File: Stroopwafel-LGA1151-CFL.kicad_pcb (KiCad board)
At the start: 2 copper layers, 2 parts

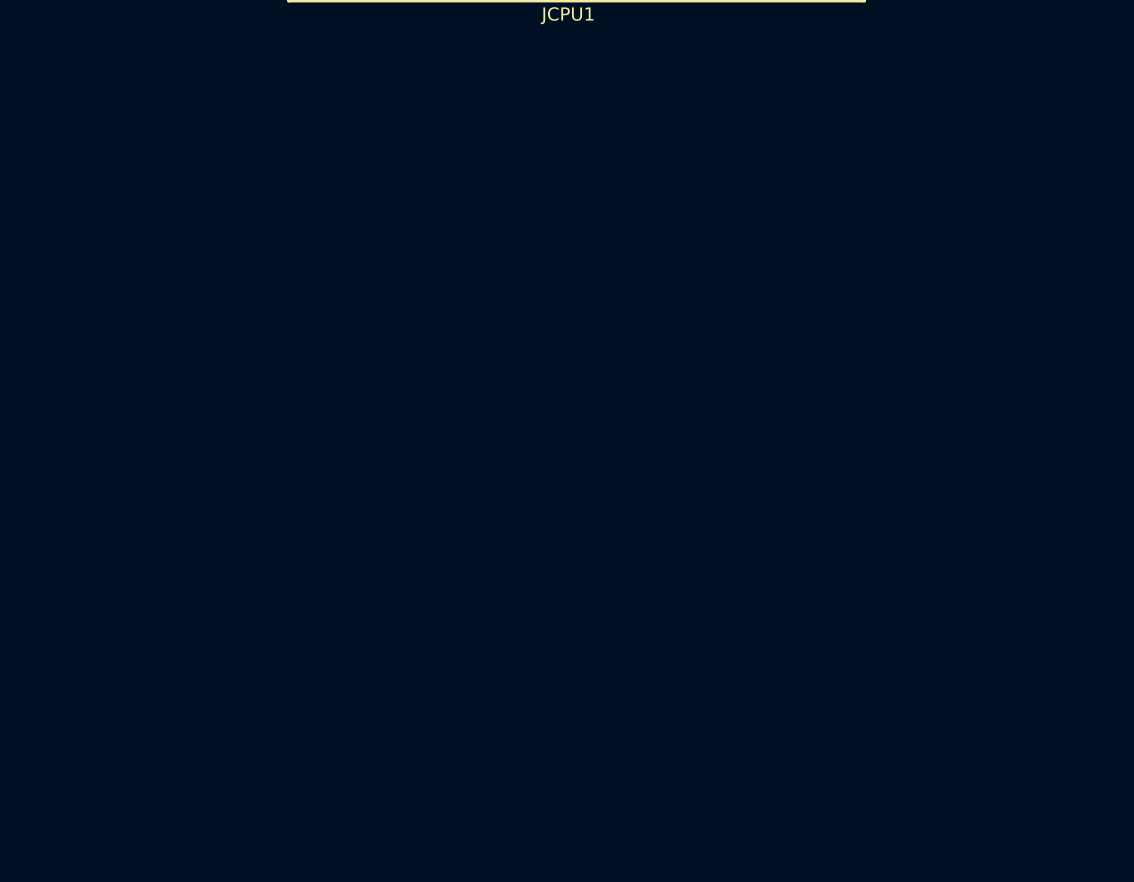
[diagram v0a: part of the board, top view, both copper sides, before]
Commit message: Added sodimm memory slots and mostly hooked them up on the schematic
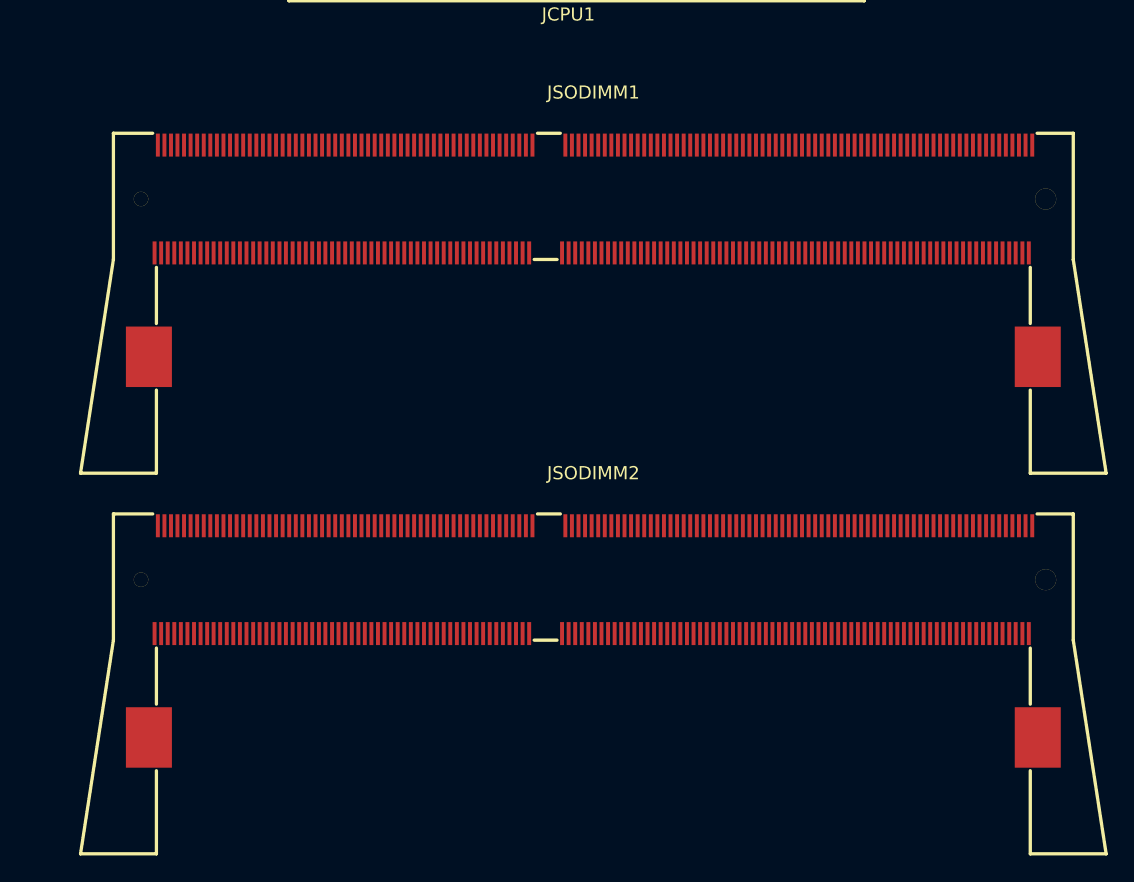
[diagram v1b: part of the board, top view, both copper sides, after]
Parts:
- added JSODIMM1: DDR4-sodimm, A-my-stuff:DDR4-sodimm-std, F.Cu at (201.9, 110.3)
- added JSODIMM2: DDR4-sodimm, A-my-stuff:DDR4-sodimm-std, F.Cu at (201.9, 139.2)
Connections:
- JCPU1 pad AD34: unconnected-(JCPU1B-DDR1_DQ_0/DDR0_DQ_16-PadAD34) -> DDR4_CH1_DQ0
- JCPU1 pad AD35: unconnected-(JCPU1B-DDR1_DQ_1/DDR0_DQ_17-PadAD35) -> DDR4_CH1_DQ1
- JCPU1 pad AE34: unconnected-(JCPU1B-DDR1_DQ_5/DDR0_DQ_21-PadAE34) -> DDR4_CH1_DQ5
- JCPU1 pad AE35: unconnected-(JCPU1B-DDR1_DQ_4/DDR0_DQ_20-PadAE35) -> DDR4_CH1_DQ4
- JCPU1 pad AE37: unconnected-(JCPU1A-DDR0_DQ_1/DDR0_DQ_1-PadAE37) -> DDR4_CH0_DQ1
- JCPU1 pad AE38: unconnected-(JCPU1A-DDR0_DQ_0/DDR0_DQ_0-PadAE38) -> DDR4_CH0_DQ0
- JCPU1 pad AE39: unconnected-(JCPU1A-DDR0_DQ_4/DDR0_DQ_4-PadAE39) -> DDR4_CH0_DQ4
- JCPU1 pad AE40: unconnected-(JCPU1A-DDR0_DQ_5/DDR0_DQ_5-PadAE40) -> DDR4_CH0_DQ5
- JCPU1 pad AE6: unconnected-(JCPU1B-DDR1_DQ_58/DDR1_DQ_58-PadAE6) -> DDR4_CH1_DQ58
- JCPU1 pad AE7: unconnected-(JCPU1B-DDR1_DQ_62/DDR1_DQ_62-PadAE7) -> DDR4_CH1_DQ62
- JCPU1 pad AF34: unconnected-(JCPU1B-DDR1_DQSN_0/DDR0_DQSN_2-PadAF34) -> DDR4_CH1_DQS0-
- JCPU1 pad AF35: unconnected-(JCPU1B-DDR1_DQSP_0/DDR0_DQSP_2-PadAF35) -> DDR4_CH1_DQS0+
- JCPU1 pad AF38: unconnected-(JCPU1A-DDR0_DQSP_0/DDR0_DQSP_0-PadAF38) -> DDR4_CH0_DQS0+
- JCPU1 pad AF39: unconnected-(JCPU1A-DDR0_DQSN_0/DDR0_DQSN_0-PadAF39) -> DDR4_CH0_DQS0-
- JCPU1 pad AF6: unconnected-(JCPU1B-DDR1_DQ_63/DDR1_DQ_63-PadAF6) -> DDR4_CH1_DQ63
- JCPU1 pad AF7: unconnected-(JCPU1B-DDR1_DQ_59/DDR1_DQ_59-PadAF7) -> DDR4_CH1_DQ59
- JCPU1 pad AG34: unconnected-(JCPU1B-DDR1_DQ_6/DDR0_DQ_22-PadAG34) -> DDR4_CH1_DQ6
- JCPU1 pad AG35: unconnected-(JCPU1B-DDR1_DQ_2/DDR0_DQ_18-PadAG35) -> DDR4_CH1_DQ2
- JCPU1 pad AG37: unconnected-(JCPU1A-DDR0_DQ_3/DDR0_DQ_3-PadAG37) -> DDR4_CH0_DQ3
- JCPU1 pad AG38: unconnected-(JCPU1A-DDR0_DQ_2/DDR0_DQ_2-PadAG38) -> DDR4_CH0_DQ2
- JCPU1 pad AG39: unconnected-(JCPU1A-DDR0_DQ_6/DDR0_DQ_6-PadAG39) -> DDR4_CH0_DQ6
- JCPU1 pad AG40: unconnected-(JCPU1A-DDR0_DQ_7/DDR0_DQ_7-PadAG40) -> DDR4_CH0_DQ7
- JCPU1 pad AG6: unconnected-(JCPU1B-DDR1_DQSN_7/DDR1_DQSN_7-PadAG6) -> DDR4_CH1_DQS7-
- JCPU1 pad AG7: unconnected-(JCPU1B-DDR1_DQSP_7/DDR1_DQSP_7-PadAG7) -> DDR4_CH1_DQS7+
- JCPU1 pad AH1: unconnected-(JCPU1A-DDR0_DQ_57/DDR1_DQ_41-PadAH1) -> DDR4_CH0_DQ57
- JCPU1 pad AH2: unconnected-(JCPU1A-DDR0_DQ_59/DDR1_DQ_43-PadAH2) -> DDR4_CH0_DQ59
- JCPU1 pad AH3: unconnected-(JCPU1A-DDR0_DQ_62/DDR1_DQ_46-PadAH3) -> DDR4_CH0_DQ62
- JCPU1 pad AH34: unconnected-(JCPU1B-DDR1_DQ_7/DDR0_DQ_23-PadAH34) -> DDR4_CH1_DQ7
- JCPU1 pad AH35: unconnected-(JCPU1B-DDR1_DQ_3/DDR0_DQ_19-PadAH35) -> DDR4_CH1_DQ3
- JCPU1 pad AH4: unconnected-(JCPU1A-DDR0_DQ_60/DDR1_DQ_44-PadAH4) -> DDR4_CH0_DQ60
- JCPU1 pad AH6: unconnected-(JCPU1B-DDR1_DQ_61/DDR1_DQ_61-PadAH6) -> DDR4_CH1_DQ61
- JCPU1 pad AH7: unconnected-(JCPU1B-DDR1_DQ_60/DDR1_DQ_60-PadAH7) -> DDR4_CH1_DQ60
- JCPU1 pad AJ2: unconnected-(JCPU1A-DDR0_DQSP_7/DDR1_DQSP_5-PadAJ2) -> DDR4_CH0_DQS7+
- JCPU1 pad AJ3: unconnected-(JCPU1A-DDR0_DQSN_7/DDR1_DQSN_5-PadAJ3) -> DDR4_CH0_DQS7-
- JCPU1 pad AJ37: unconnected-(JCPU1A-DDR0_DQ_9/DDR0_DQ_9-PadAJ37) -> DDR4_CH0_DQ9
- JCPU1 pad AJ38: unconnected-(JCPU1A-DDR0_DQ_8/DDR0_DQ_8-PadAJ38) -> DDR4_CH0_DQ8
- JCPU1 pad AJ39: unconnected-(JCPU1A-DDR0_DQ_13/DDR0_DQ_13-PadAJ39) -> DDR4_CH0_DQ13
- JCPU1 pad AJ40: unconnected-(JCPU1A-DDR0_DQ_12/DDR0_DQ_12-PadAJ40) -> DDR4_CH0_DQ12
- JCPU1 pad AJ6: unconnected-(JCPU1B-DDR1_DQ_56/DDR1_DQ_56-PadAJ6) -> DDR4_CH1_DQ56
- JCPU1 pad AJ7: unconnected-(JCPU1B-DDR1_DQ_57/DDR1_DQ_57-PadAJ7) -> DDR4_CH1_DQ57
- JCPU1 pad AK1: unconnected-(JCPU1A-DDR0_DQ_63/DDR1_DQ_47-PadAK1) -> DDR4_CH0_DQ63
- JCPU1 pad AK2: unconnected-(JCPU1A-DDR0_DQ_61/DDR1_DQ_45-PadAK2) -> DDR4_CH0_DQ61
- JCPU1 pad AK3: unconnected-(JCPU1A-DDR0_DQ_56/DDR1_DQ_40-PadAK3) -> DDR4_CH0_DQ56
- JCPU1 pad AK31: unconnected-(JCPU1B-DDR1_DQ_14/DDR0_DQ_30-PadAK31) -> DDR4_CH1_DQ14
- JCPU1 pad AK32: unconnected-(JCPU1B-DDR1_DQ_10/DDR0_DQ_26-PadAK32) -> DDR4_CH1_DQ10
- JCPU1 pad AK33: unconnected-(JCPU1B-DDR1_DQSN_1/DDR0_DQSN_3-PadAK33) -> DDR4_CH1_DQS1-
- JCPU1 pad AK34: unconnected-(JCPU1B-DDR1_DQ_12/DDR0_DQ_28-PadAK34) -> DDR4_CH1_DQ12
- JCPU1 pad AK35: unconnected-(JCPU1B-DDR1_DQ_8/DDR0_DQ_24-PadAK35) -> DDR4_CH1_DQ8
- JCPU1 pad AK38: unconnected-(JCPU1A-DDR0_DQSP_1/DDR0_DQSP_1-PadAK38) -> DDR4_CH0_DQS1+
- JCPU1 pad AK39: unconnected-(JCPU1A-DDR0_DQSN_1/DDR0_DQSN_1-PadAK39) -> DDR4_CH0_DQS1-
- JCPU1 pad AK4: unconnected-(JCPU1A-DDR0_DQ_58/DDR1_DQ_42-PadAK4) -> DDR4_CH0_DQ58
- JCPU1 pad AL10: unconnected-(JCPU1B-DDR1_DQ_49/DDR1_DQ_49-PadAL10) -> DDR4_CH1_DQ49
- JCPU1 pad AL12: unconnected-(JCPU1B-DDR1_DQ_39/DDR1_DQ_23-PadAL12) -> DDR4_CH1_DQ39
- JCPU1 pad AL13: unconnected-(JCPU1B-DDR1_DQ_35/DDR1_DQ_19-PadAL13) -> DDR4_CH1_DQ35
- JCPU1 pad AL16: unconnected-(JCPU1B-DDR1_ODT_1-PadAL16) -> DDR4_CH1_ODT1
- JCPU1 pad AL17: unconnected-(JCPU1B-DDR1_MA_14-PadAL17) -> DDR4_CH1_A14_WE#
- JCPU1 pad AL18: unconnected-(JCPU1B-DDR1_BA_0-PadAL18) -> DDR4_CH1_BA0
- JCPU1 pad AL19: unconnected-(JCPU1B-DDR1_MA_0-PadAL19) -> DDR4_CH1_A0
- JCPU1 pad AL20: unconnected-(JCPU1B-DDR1_PAR-PadAL20) -> DDR4_CH1_Parity
- JCPU1 pad AL22: unconnected-(JCPU1B-DDR1_MA_1-PadAL22) -> DDR4_CH1_A1
- JCPU1 pad AL23: unconnected-(JCPU1B-DDR1_MA_5-PadAL23) -> DDR4_CH1_A5
- JCPU1 pad AL25: unconnected-(JCPU1B-DDR1_ECC_6-PadAL25) -> DDR4_CH1_ECC6
- JCPU1 pad AL26: unconnected-(JCPU1B-DDR1_ECC_7-PadAL26) -> DDR4_CH1_ECC7
- JCPU1 pad AL28: unconnected-(JCPU1B-DDR1_DQ_29/DDR0_DQ_61-PadAL28) -> DDR4_CH1_DQ29
- JCPU1 pad AL29: unconnected-(JCPU1B-DDR1_DQ_24/DDR0_DQ_56-PadAL29) -> DDR4_CH1_DQ24
- JCPU1 pad AL31: unconnected-(JCPU1B-DDR1_DQ_15/DDR0_DQ_31-PadAL31) -> DDR4_CH1_DQ15
- JCPU1 pad AL32: unconnected-(JCPU1B-DDR1_DQ_11/DDR0_DQ_27-PadAL32) -> DDR4_CH1_DQ11
- JCPU1 pad AL33: unconnected-(JCPU1B-DDR1_DQSP_1/DDR0_DQSP_3-PadAL33) -> DDR4_CH1_DQS1+
- JCPU1 pad AL34: unconnected-(JCPU1B-DDR1_DQ_13/DDR0_DQ_29-PadAL34) -> DDR4_CH1_DQ13
- JCPU1 pad AL35: unconnected-(JCPU1B-DDR1_DQ_9/DDR0_DQ_25-PadAL35) -> DDR4_CH1_DQ9
- JCPU1 pad AL37: unconnected-(JCPU1A-DDR0_DQ_11/DDR0_DQ_11-PadAL37) -> DDR4_CH0_DQ11
- JCPU1 pad AL38: unconnected-(JCPU1A-DDR0_DQ_10/DDR0_DQ_10-PadAL38) -> DDR4_CH0_DQ10
- JCPU1 pad AL39: unconnected-(JCPU1A-DDR0_DQ_14/DDR0_DQ_14-PadAL39) -> DDR4_CH0_DQ14
- JCPU1 pad AL40: unconnected-(JCPU1A-DDR0_DQ_15/DDR0_DQ_15-PadAL40) -> DDR4_CH0_DQ15
- JCPU1 pad AL6: unconnected-(JCPU1B-DDR1_DQ_55/DDR1_DQ_55-PadAL6) -> DDR4_CH1_DQ55
- JCPU1 pad AL7: unconnected-(JCPU1B-DDR1_DQ_51/DDR1_DQ_51-PadAL7) -> DDR4_CH1_DQ51
- JCPU1 pad AL8: unconnected-(JCPU1B-DDR1_DQSP_6/DDR1_DQSP_6-PadAL8) -> DDR4_CH1_DQS6+
- JCPU1 pad AL9: unconnected-(JCPU1B-DDR1_DQ_53/DDR1_DQ_53-PadAL9) -> DDR4_CH1_DQ53
- JCPU1 pad AM1: unconnected-(JCPU1A-DDR0_DQ_55/DDR1_DQ_39-PadAM1) -> DDR4_CH0_DQ55
- JCPU1 pad AM10: unconnected-(JCPU1B-DDR1_DQ_48/DDR1_DQ_48-PadAM10) -> DDR4_CH1_DQ48
- JCPU1 pad AM12: unconnected-(JCPU1B-DDR1_DQ_38/DDR1_DQ_22-PadAM12) -> DDR4_CH1_DQ38
- JCPU1 pad AM13: unconnected-(JCPU1B-DDR1_DQ_34/DDR1_DQ_18-PadAM13) -> DDR4_CH1_DQ34
- JCPU1 pad AM16: unconnected-(JCPU1B-DDR1_ODT_0-PadAM16) -> DDR4_CH1_ODT0
- JCPU1 pad AM18: unconnected-(JCPU1B-DDR1_BA_1-PadAM18) -> DDR4_CH1_BA1
- JCPU1 pad AM2: unconnected-(JCPU1A-DDR0_DQ_53/DDR1_DQ_37-PadAM2) -> DDR4_CH0_DQ53
- JCPU1 pad AM20: unconnected-(JCPU1B-DDR1_CKP_0-PadAM20) -> DDR4_CH1_CLK0+
- JCPU1 pad AM21: unconnected-(JCPU1B-DDR1_CKN_0-PadAM21) -> DDR4_CH1_CLK0-
- JCPU1 pad AM22: unconnected-(JCPU1B-DDR1_MA_2-PadAM22) -> DDR4_CH1_A2
- JCPU1 pad AM23: unconnected-(JCPU1B-DDR1_MA_3-PadAM23) -> DDR4_CH1_A3
- JCPU1 pad AM25: unconnected-(JCPU1B-DDR1_ECC_3-PadAM25) -> DDR4_CH1_ECC3
- JCPU1 pad AM26: unconnected-(JCPU1B-DDR1_ECC_2-PadAM26) -> DDR4_CH1_ECC2
- JCPU1 pad AM28: unconnected-(JCPU1B-DDR1_DQ_28/DDR0_DQ_60-PadAM28) -> DDR4_CH1_DQ28
- JCPU1 pad AM29: unconnected-(JCPU1B-DDR1_DQ_25/DDR0_DQ_57-PadAM29) -> DDR4_CH1_DQ25
- JCPU1 pad AM3: unconnected-(JCPU1A-DDR0_DQ_51/DDR1_DQ_35-PadAM3) -> DDR4_CH0_DQ51
- JCPU1 pad AM4: unconnected-(JCPU1A-DDR0_DQ_49/DDR1_DQ_33-PadAM4) -> DDR4_CH0_DQ49
- JCPU1 pad AM6: unconnected-(JCPU1B-DDR1_DQ_54/DDR1_DQ_54-PadAM6) -> DDR4_CH1_DQ54
- JCPU1 pad AM7: unconnected-(JCPU1B-DDR1_DQ_50/DDR1_DQ_50-PadAM7) -> DDR4_CH1_DQ50
- JCPU1 pad AM8: unconnected-(JCPU1B-DDR1_DQSN_6/DDR1_DQSN_6-PadAM8) -> DDR4_CH1_DQS6-
- JCPU1 pad AM9: unconnected-(JCPU1B-DDR1_DQ_52/DDR1_DQ_52-PadAM9) -> DDR4_CH1_DQ52
- JCPU1 pad AN12: unconnected-(JCPU1B-DDR1_DQSP_4/DDR1_DQSP_2-PadAN12) -> DDR4_CH1_DQS4+
- JCPU1 pad AN13: unconnected-(JCPU1B-DDR1_DQSN_4/DDR1_DQSN_2-PadAN13) -> DDR4_CH1_DQS4-
- JCPU1 pad AN15: unconnected-(JCPU1B-DDR1_CS#_1-PadAN15) -> DDR4_CH1_CS1#
- JCPU1 pad AN18: unconnected-(JCPU1B-DDR1_MA_16-PadAN18) -> DDR4_CH1_A16_RAS#
- JCPU1 pad AN2: unconnected-(JCPU1A-DDR0_DQSP_6/DDR1_DQSP_4-PadAN2) -> DDR4_CH0_DQS6+
- JCPU1 pad AN25: unconnected-(JCPU1B-DDR1_DQSP_8/DDR1_DQSP_8-PadAN25) -> DDR4_CH1_DQS8+
- JCPU1 pad AN26: unconnected-(JCPU1B-DDR1_DQSN_8/DDR1_DQSN_8-PadAN26) -> DDR4_CH1_DQS8-
- JCPU1 pad AN28: unconnected-(JCPU1B-DDR1_DQSP_3/DDR0_DQSP_7-PadAN28) -> DDR4_CH1_DQS3+
- JCPU1 pad AN29: unconnected-(JCPU1B-DDR1_DQSN_3/DDR0_DQSN_7-PadAN29) -> DDR4_CH1_DQS3-
- JCPU1 pad AN3: unconnected-(JCPU1A-DDR0_DQSN_6/DDR1_DQSN_4-PadAN3) -> DDR4_CH0_DQS6-
- JCPU1 pad AN31: unconnected-(JCPU1B-DDR1_DQ_22/DDR0_DQ_54-PadAN31) -> DDR4_CH1_DQ22
- JCPU1 pad AN32: unconnected-(JCPU1B-DDR1_DQ_18/DDR0_DQ_50-PadAN32) -> DDR4_CH1_DQ18
- JCPU1 pad AN33: unconnected-(JCPU1B-DDR1_DQSN_2/DDR0_DQSN_6-PadAN33) -> DDR4_CH1_DQS2-
- JCPU1 pad AN34: unconnected-(JCPU1B-DDR1_DQ_20/DDR0_DQ_52-PadAN34) -> DDR4_CH1_DQ20
- JCPU1 pad AN35: unconnected-(JCPU1B-DDR1_DQ_17/DDR0_DQ_49-PadAN35) -> DDR4_CH1_DQ17
- JCPU1 pad AN37: unconnected-(JCPU1A-DDR0_DQ_21/DDR0_DQ_37-PadAN37) -> DDR4_CH0_DQ21
- JCPU1 pad AN38: unconnected-(JCPU1A-DDR0_DQ_16/DDR0_DQ_32-PadAN38) -> DDR4_CH0_DQ16
- JCPU1 pad AN39: unconnected-(JCPU1A-DDR0_DQ_20/DDR0_DQ_36-PadAN39) -> DDR4_CH0_DQ20
- JCPU1 pad AN40: unconnected-(JCPU1A-DDR0_DQ_17/DDR0_DQ_33-PadAN40) -> DDR4_CH0_DQ17
- JCPU1 pad AP1: unconnected-(JCPU1A-DDR0_DQ_54/DDR1_DQ_38-PadAP1) -> DDR4_CH0_DQ54
- JCPU1 pad AP10: unconnected-(JCPU1B-DDR1_DQ_40/DDR1_DQ_24-PadAP10) -> DDR4_CH1_DQ40
- JCPU1 pad AP12: unconnected-(JCPU1B-DDR1_DQ_33/DDR1_DQ_17-PadAP12) -> DDR4_CH1_DQ33
- JCPU1 pad AP13: unconnected-(JCPU1B-DDR1_DQ_37/DDR1_DQ_21-PadAP13) -> DDR4_CH1_DQ37
- JCPU1 pad AP16: unconnected-(JCPU1B-DDR1_MA_15-PadAP16) -> DDR4_CH1_A15_CAS#
- JCPU1 pad AP17: unconnected-(JCPU1B-DDR1_CS#_0-PadAP17) -> DDR4_CH1_CS0#
- JCPU1 pad AP18: unconnected-(JCPU1B-DDR1_MA_10-PadAP18) -> DDR4_CH1_A10
- JCPU1 pad AP2: unconnected-(JCPU1A-DDR0_DQ_48/DDR1_DQ_32-PadAP2) -> DDR4_CH0_DQ48
- JCPU1 pad AP21: unconnected-(JCPU1B-DDR1_CKN_1-PadAP21) -> DDR4_CH1_CLK1-
- JCPU1 pad AP22: unconnected-(JCPU1B-DDR1_CKP_1-PadAP22) -> DDR4_CH1_CLK1+
- JCPU1 pad AP23: unconnected-(JCPU1B-DDR1_MA_4-PadAP23) -> DDR4_CH1_A4
- JCPU1 pad AP25: unconnected-(JCPU1B-DDR1_ECC_5-PadAP25) -> DDR4_CH1_ECC5
- JCPU1 pad AP26: unconnected-(JCPU1B-DDR1_ECC_4-PadAP26) -> DDR4_CH1_ECC4
- JCPU1 pad AP28: unconnected-(JCPU1B-DDR1_DQ_31/DDR0_DQ_63-PadAP28) -> DDR4_CH1_DQ31
- JCPU1 pad AP29: unconnected-(JCPU1B-DDR1_DQ_26/DDR0_DQ_58-PadAP29) -> DDR4_CH1_DQ26
- JCPU1 pad AP3: unconnected-(JCPU1A-DDR0_DQ_50/DDR1_DQ_34-PadAP3) -> DDR4_CH0_DQ50
- JCPU1 pad AP31: unconnected-(JCPU1B-DDR1_DQ_23/DDR0_DQ_55-PadAP31) -> DDR4_CH1_DQ23
- JCPU1 pad AP32: unconnected-(JCPU1B-DDR1_DQ_19/DDR0_DQ_51-PadAP32) -> DDR4_CH1_DQ19
- JCPU1 pad AP33: unconnected-(JCPU1B-DDR1_DQSP_2/DDR0_DQSP_6-PadAP33) -> DDR4_CH1_DQS2+
- JCPU1 pad AP34: unconnected-(JCPU1B-DDR1_DQ_21/DDR0_DQ_53-PadAP34) -> DDR4_CH1_DQ21
- JCPU1 pad AP35: unconnected-(JCPU1B-DDR1_DQ_16/DDR0_DQ_48-PadAP35) -> DDR4_CH1_DQ16
- JCPU1 pad AP38: unconnected-(JCPU1A-DDR0_DQSP_2/DDR0_DQSP_4-PadAP38) -> DDR4_CH0_DQS2+
- JCPU1 pad AP39: unconnected-(JCPU1A-DDR0_DQSN_2/DDR0_DQSN_4-PadAP39) -> DDR4_CH0_DQS2-
- JCPU1 pad AP4: unconnected-(JCPU1A-DDR0_DQ_52/DDR1_DQ_36-PadAP4) -> DDR4_CH0_DQ52
- JCPU1 pad AP6: unconnected-(JCPU1B-DDR1_DQ_47/DDR1_DQ_31-PadAP6) -> DDR4_CH1_DQ47
- JCPU1 pad AP7: unconnected-(JCPU1B-DDR1_DQ_43/DDR1_DQ_27-PadAP7) -> DDR4_CH1_DQ43
- JCPU1 pad AP8: unconnected-(JCPU1B-DDR1_DQSP_5/DDR1_DQSP_3-PadAP8) -> DDR4_CH1_DQS5+
- JCPU1 pad AP9: unconnected-(JCPU1B-DDR1_DQ_45/DDR1_DQ_29-PadAP9) -> DDR4_CH1_DQ45
- JCPU1 pad AR10: unconnected-(JCPU1B-DDR1_DQ_41/DDR1_DQ_25-PadAR10) -> DDR4_CH1_DQ41
- JCPU1 pad AR12: unconnected-(JCPU1B-DDR1_DQ_32/DDR1_DQ_16-PadAR12) -> DDR4_CH1_DQ32
- JCPU1 pad AR13: unconnected-(JCPU1B-DDR1_DQ_36/DDR1_DQ_20-PadAR13) -> DDR4_CH1_DQ36
- JCPU1 pad AR15: unconnected-(JCPU1B-DDR1_MA_13-PadAR15) -> DDR4_CH1_A13
- JCPU1 pad AR25: unconnected-(JCPU1B-DDR1_ECC_0-PadAR25) -> DDR4_CH1_ECC0
- JCPU1 pad AR26: unconnected-(JCPU1B-DDR1_ECC_1-PadAR26) -> DDR4_CH1_ECC1
- JCPU1 pad AR28: unconnected-(JCPU1B-DDR1_DQ_30/DDR0_DQ_62-PadAR28) -> DDR4_CH1_DQ30
- JCPU1 pad AR29: unconnected-(JCPU1B-DDR1_DQ_27/DDR0_DQ_59-PadAR29) -> DDR4_CH1_DQ27
- JCPU1 pad AR37: unconnected-(JCPU1A-DDR0_DQ_19/DDR0_DQ_35-PadAR37) -> DDR4_CH0_DQ19
- JCPU1 pad AR38: unconnected-(JCPU1A-DDR0_DQ_18/DDR0_DQ_34-PadAR38) -> DDR4_CH0_DQ18
- JCPU1 pad AR39: unconnected-(JCPU1A-DDR0_DQ_22/DDR0_DQ_38-PadAR39) -> DDR4_CH0_DQ22
- JCPU1 pad AR40: unconnected-(JCPU1A-DDR0_DQ_23/DDR0_DQ_39-PadAR40) -> DDR4_CH0_DQ23
- JCPU1 pad AR6: unconnected-(JCPU1B-DDR1_DQ_46/DDR1_DQ_30-PadAR6) -> DDR4_CH1_DQ46
- JCPU1 pad AR7: unconnected-(JCPU1B-DDR1_DQ_42/DDR1_DQ_26-PadAR7) -> DDR4_CH1_DQ42
- JCPU1 pad AR8: unconnected-(JCPU1B-DDR1_DQSN_5/DDR1_DQSN_3-PadAR8) -> DDR4_CH1_DQS5-
- JCPU1 pad AR9: unconnected-(JCPU1B-DDR1_DQ_44/DDR1_DQ_28-PadAR9) -> DDR4_CH1_DQ44
- JCPU1 pad AT1: unconnected-(JCPU1A-DDR0_DQ_42/DDR1_DQ_10-PadAT1) -> DDR4_CH0_DQ42
- JCPU1 pad AT19: unconnected-(JCPU1A-DDR0_MA_4-PadAT19) -> DDR4_CH0_A4
- JCPU1 pad AT2: unconnected-(JCPU1A-DDR0_DQ_43/DDR1_DQ_11-PadAT2) -> DDR4_CH0_DQ43
- JCPU1 pad AT20: unconnected-(JCPU1A-DDR0_MA_8-PadAT20) -> DDR4_CH0_A8
- JCPU1 pad AT22: unconnected-(JCPU1A-DDR0_MA_9-PadAT22) -> DDR4_CH0_A9
- JCPU1 pad AT23: unconnected-(JCPU1A-DDR0_ALERT#-PadAT23) -> DDR4_CH0_Alert#
- JCPU1 pad AT3: unconnected-(JCPU1A-DDR0_DQ_47/DDR1_DQ_15-PadAT3) -> DDR4_CH0_DQ47
- JCPU1 pad AT33: unconnected-(JCPU1A-DDR0_ECC_1-PadAT33) -> DDR4_CH0_ECC1
- JCPU1 pad AT35: unconnected-(JCPU1A-DDR0_DQ_30/DDR0_DQ_46-PadAT35) -> DDR4_CH0_DQ30
- JCPU1 pad AT4: unconnected-(JCPU1A-DDR0_DQ_46/DDR1_DQ_14-PadAT4) -> DDR4_CH0_DQ46
- JCPU1 pad AU11: unconnected-(JCPU1A-DDR0_CS#_1-PadAU11) -> DDR4_CH0_CS1#
- JCPU1 pad AU14: unconnected-(JCPU1A-DDR0_ODT_1-PadAU14) -> DDR4_CH0_ODT1
- JCPU1 pad AU17: unconnected-(JCPU1A-DDR0_MA_2-PadAU17) -> DDR4_CH0_A2
- JCPU1 pad AU18: unconnected-(JCPU1A-DDR0_MA_1-PadAU18) -> DDR4_CH0_A1
- JCPU1 pad AU2: unconnected-(JCPU1A-DDR0_DQSP_5/DDR1_DQSP_1-PadAU2) -> DDR4_CH0_DQS5+
- JCPU1 pad AU20: unconnected-(JCPU1A-DDR0_MA_5-PadAU20) -> DDR4_CH0_A5
- JCPU1 pad AU21: unconnected-(JCPU1A-DDR0_MA_7-PadAU21) -> DDR4_CH0_A7
- JCPU1 pad AU22: unconnected-(JCPU1A-DDR0_MA_11-PadAU22) -> DDR4_CH0_A11
- JCPU1 pad AU24: unconnected-(JCPU1A-DDR0_ACT#-PadAU24) -> DDR4_CH0_ACT#
- JCPU1 pad AU26: unconnected-(JCPU1B-DDR1_MA_8-PadAU26) -> DDR4_CH1_A8
- JCPU1 pad AU27: unconnected-(JCPU1B-DDR1_MA_11-PadAU27) -> DDR4_CH1_A11
- JCPU1 pad AU28: unconnected-(JCPU1B-DDR1_ACT#-PadAU28) -> DDR4_CH1_ACT#
- JCPU1 pad AU3: unconnected-(JCPU1A-DDR0_DQSN_5/DDR1_DQSN_1-PadAU3) -> DDR4_CH0_DQS5-
- JCPU1 pad AU31: unconnected-(JCPU1A-DDR0_ECC_4-PadAU31) -> DDR4_CH0_ECC4
- JCPU1 pad AU32: unconnected-(JCPU1A-DDR0_DQSN_8/DDR0_DQSN_8-PadAU32) -> DDR4_CH0_DQS8-
- JCPU1 pad AU33: unconnected-(JCPU1A-DDR0_ECC_0-PadAU33) -> DDR4_CH0_ECC0
- JCPU1 pad AU35: unconnected-(JCPU1A-DDR0_DQ_31/DDR0_DQ_47-PadAU35) -> DDR4_CH0_DQ31
- JCPU1 pad AU36: unconnected-(JCPU1A-DDR0_DQSN_3/DDR0_DQSN_5-PadAU36) -> DDR4_CH0_DQS3-
- JCPU1 pad AU37: unconnected-(JCPU1A-DDR0_DQ_28/DDR0_DQ_44-PadAU37) -> DDR4_CH0_DQ28
- JCPU1 pad AU38: unconnected-(JCPU1A-DDR0_DQ_25/DDR0_DQ_41-PadAU38) -> DDR4_CH0_DQ25
- JCPU1 pad AU6: unconnected-(JCPU1A-DDR0_DQ_35/DDR1_DQ_3-PadAU6) -> DDR4_CH0_DQ35
- JCPU1 pad AU8: unconnected-(JCPU1A-DDR0_DQ_36/DDR1_DQ_4-PadAU8) -> DDR4_CH0_DQ36
- JCPU1 pad AV12: unconnected-(JCPU1A-DDR0_MA_13-PadAV12) -> DDR4_CH0_A13
- JCPU1 pad AV14: unconnected-(JCPU1A-DDR0_MA_14-PadAV14) -> DDR4_CH0_A14_WE#
- JCPU1 pad AV15: unconnected-(JCPU1A-DDR0_BA_1-PadAV15) -> DDR4_CH0_BA1
- JCPU1 pad AV18: unconnected-(JCPU1A-DDR0_CKN_0-PadAV18) -> DDR4_CH0_CLK0-
- JCPU1 pad AV19: unconnected-(JCPU1A-DDR0_MA_3-PadAV19) -> DDR4_CH0_A3
- JCPU1 pad AV20: unconnected-(JCPU1A-DDR0_MA_6-PadAV20) -> DDR4_CH0_A6
- JCPU1 pad AV22: unconnected-(JCPU1A-DDR0_MA_12-PadAV22) -> DDR4_CH0_A12
- JCPU1 pad AV23: unconnected-(JCPU1A-DDR0_BG_1-PadAV23) -> DDR4_CH0_BG1
- JCPU1 pad AV27: unconnected-(JCPU1B-DDR1_MA_12-PadAV27) -> DDR4_CH1_A12
- JCPU1 pad AV29: unconnected-(JCPU1B-DDR1_CKE_1-PadAV29) -> DDR4_CH1_CKE1
- JCPU1 pad AV3: unconnected-(JCPU1A-DDR0_DQ_44/DDR1_DQ_12-PadAV3) -> DDR4_CH0_DQ44
- JCPU1 pad AV31: unconnected-(JCPU1A-DDR0_ECC_3-PadAV31) -> DDR4_CH0_ECC3
- JCPU1 pad AV32: unconnected-(JCPU1A-DDR0_DQSP_8/DDR0_DQSP_8-PadAV32) -> DDR4_CH0_DQS8+
- JCPU1 pad AV33: unconnected-(JCPU1A-DDR0_ECC_5-PadAV33) -> DDR4_CH0_ECC5
- JCPU1 pad AV35: unconnected-(JCPU1A-DDR0_DQ_26/DDR0_DQ_42-PadAV35) -> DDR4_CH0_DQ26
- JCPU1 pad AV36: unconnected-(JCPU1A-DDR0_DQSP_3/DDR0_DQSP_5-PadAV36) -> DDR4_CH0_DQS3+
- JCPU1 pad AV37: unconnected-(JCPU1A-DDR0_DQ_29/DDR0_DQ_45-PadAV37) -> DDR4_CH0_DQ29
- JCPU1 pad AV4: unconnected-(JCPU1A-DDR0_DQ_41/DDR1_DQ_9-PadAV4) -> DDR4_CH0_DQ41
- JCPU1 pad AV6: unconnected-(JCPU1A-DDR0_DQ_34/DDR1_DQ_2-PadAV6) -> DDR4_CH0_DQ34
- JCPU1 pad AV7: unconnected-(JCPU1A-DDR0_DQSP_4/DDR1_DQSP_0-PadAV7) -> DDR4_CH0_DQS4+
- JCPU1 pad AV8: unconnected-(JCPU1A-DDR0_DQ_37/DDR1_DQ_5-PadAV8) -> DDR4_CH0_DQ37
- JCPU1 pad AW11: unconnected-(JCPU1A-DDR0_ODT_0-PadAW11) -> DDR4_CH0_ODT0
- JCPU1 pad AW12: unconnected-(JCPU1A-DDR0_CS#_0-PadAW12) -> DDR4_CH0_CS0#
- JCPU1 pad AW13: unconnected-(JCPU1A-DDR0_MA_16-PadAW13) -> DDR4_CH0_A16_RAS#
- JCPU1 pad AW15: unconnected-(JCPU1A-DDR0_MA_0-PadAW15) -> DDR4_CH0_A0
- JCPU1 pad AW17: unconnected-(JCPU1A-DDR0_CKP_1-PadAW17) -> DDR4_CH0_CLK1+
- JCPU1 pad AW18: unconnected-(JCPU1A-DDR0_CKP_0-PadAW18) -> DDR4_CH0_CLK0+
- JCPU1 pad AW23: unconnected-(JCPU1A-DDR0_BG_0-PadAW23) -> DDR4_CH0_BG0
- JCPU1 pad AW24: unconnected-(JCPU1A-DDR0_CKE_1-PadAW24) -> DDR4_CH0_CKE1
- JCPU1 pad AW26: unconnected-(JCPU1B-DDR1_MA_6-PadAW26) -> DDR4_CH1_A6
- JCPU1 pad AW27: unconnected-(JCPU1B-DDR1_MA_9-PadAW27) -> DDR4_CH1_A9
- JCPU1 pad AW28: unconnected-(JCPU1B-DDR1_BG_0-PadAW28) -> DDR4_CH1_BG0
- JCPU1 pad AW31: unconnected-(JCPU1A-DDR0_ECC_6-PadAW31) -> DDR4_CH0_ECC6
- JCPU1 pad AW33: unconnected-(JCPU1A-DDR0_ECC_2-PadAW33) -> DDR4_CH0_ECC2
- JCPU1 pad AW35: unconnected-(JCPU1A-DDR0_DQ_27/DDR0_DQ_43-PadAW35) -> DDR4_CH0_DQ27
- JCPU1 pad AW37: unconnected-(JCPU1A-DDR0_DQ_24/DDR0_DQ_40-PadAW37) -> DDR4_CH0_DQ24
- JCPU1 pad AW4: unconnected-(JCPU1A-DDR0_DQ_45/DDR1_DQ_13-PadAW4) -> DDR4_CH0_DQ45
- JCPU1 pad AW6: unconnected-(JCPU1A-DDR0_DQ_38/DDR1_DQ_6-PadAW6) -> DDR4_CH0_DQ38
- JCPU1 pad AW7: unconnected-(JCPU1A-DDR0_DQSN_4/DDR1_DQSN_0-PadAW7) -> DDR4_CH0_DQS4-
- JCPU1 pad AW8: unconnected-(JCPU1A-DDR0_DQ_33/DDR1_DQ_1-PadAW8) -> DDR4_CH0_DQ33
- JCPU1 pad AY11: unconnected-(JCPU1A-DDR0_MA_15-PadAY11) -> DDR4_CH0_A15_CAS#
- JCPU1 pad AY13: unconnected-(JCPU1A-DDR0_BA_0-PadAY13) -> DDR4_CH0_BA0
- JCPU1 pad AY14: unconnected-(JCPU1A-DDR0_MA_10-PadAY14) -> DDR4_CH0_A10
- JCPU1 pad AY15: unconnected-(JCPU1A-DDR0_PAR-PadAY15) -> DDR4_CH0_Parity
- JCPU1 pad AY17: unconnected-(JCPU1A-DDR0_CKN_1-PadAY17) -> DDR4_CH0_CLK1-
- JCPU1 pad AY24: unconnected-(JCPU1A-DDR0_CKE_0-PadAY24) -> DDR4_CH0_CKE0
- JCPU1 pad AY25: unconnected-(JCPU1B-DDR1_ALERT#-PadAY25) -> DDR4_CH1_Alert#
- JCPU1 pad AY26: unconnected-(JCPU1B-DDR1_MA_7-PadAY26) -> DDR4_CH1_A7
- JCPU1 pad AY28: unconnected-(JCPU1B-DDR1_BG_1-PadAY28) -> DDR4_CH1_BG1
- JCPU1 pad AY29: unconnected-(JCPU1B-DDR1_CKE_0-PadAY29) -> DDR4_CH1_CKE0
- JCPU1 pad AY31: unconnected-(JCPU1A-DDR0_ECC_7-PadAY31) -> DDR4_CH0_ECC7
- JCPU1 pad AY4: unconnected-(JCPU1A-DDR0_DQ_40/DDR1_DQ_8-PadAY4) -> DDR4_CH0_DQ40
- JCPU1 pad AY6: unconnected-(JCPU1A-DDR0_DQ_39/DDR1_DQ_7-PadAY6) -> DDR4_CH0_DQ39
- JCPU1 pad AY8: unconnected-(JCPU1A-DDR0_DQ_32/DDR1_DQ_0-PadAY8) -> DDR4_CH0_DQ32

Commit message: Added pretty colors
pretty fun to do
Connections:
- JSODIMM1 pad 1: unconnected-(JSODIMM1-VSS-Pad1) -> GND
- JSODIMM1 pad 10: unconnected-(JSODIMM1-VSS-Pad10) -> GND
- JSODIMM1 pad 102: unconnected-(JSODIMM1-VSS-Pad102) -> GND
- JSODIMM1 pad 103: unconnected-(JSODIMM1-VSS-Pad103) -> GND
- JSODIMM1 pad 106: unconnected-(JSODIMM1-VSS-Pad106) -> GND
- JSODIMM1 pad 107: unconnected-(JSODIMM1-VSS-Pad107) -> GND
- JSODIMM1 pad 14: unconnected-(JSODIMM1-VSS-Pad14) -> GND
- JSODIMM1 pad 15: unconnected-(JSODIMM1-VSS-Pad15) -> GND
- JSODIMM1 pad 167: unconnected-(JSODIMM1-VSS-Pad167) -> GND
- JSODIMM1 pad 168: unconnected-(JSODIMM1-VSS-Pad168) -> GND
- JSODIMM1 pad 171: unconnected-(JSODIMM1-VSS-Pad171) -> GND
- JSODIMM1 pad 172: unconnected-(JSODIMM1-VSS-Pad172) -> GND
- JSODIMM1 pad 175: unconnected-(JSODIMM1-VSS-Pad175) -> GND
- JSODIMM1 pad 176: unconnected-(JSODIMM1-VSS-Pad176) -> GND
- JSODIMM1 pad 18: unconnected-(JSODIMM1-VSS-Pad18) -> GND
- JSODIMM1 pad 180: unconnected-(JSODIMM1-VSS-Pad180) -> GND
- JSODIMM1 pad 181: unconnected-(JSODIMM1-VSS-Pad181) -> GND
- JSODIMM1 pad 184: unconnected-(JSODIMM1-VSS-Pad184) -> GND
- JSODIMM1 pad 185: unconnected-(JSODIMM1-VSS-Pad185) -> GND
- JSODIMM1 pad 188: unconnected-(JSODIMM1-VSS-Pad188) -> GND
- JSODIMM1 pad 189: unconnected-(JSODIMM1-VSS-Pad189) -> GND
- JSODIMM1 pad 19: unconnected-(JSODIMM1-VSS-Pad19) -> GND
- JSODIMM1 pad 192: unconnected-(JSODIMM1-VSS-Pad192) -> GND
- JSODIMM1 pad 193: unconnected-(JSODIMM1-VSS-Pad193) -> GND
- JSODIMM1 pad 196: unconnected-(JSODIMM1-VSS-Pad196) -> GND
- JSODIMM1 pad 197: unconnected-(JSODIMM1-VSS-Pad197) -> GND
- JSODIMM1 pad 2: unconnected-(JSODIMM1-VSS-Pad2) -> GND
- JSODIMM1 pad 201: unconnected-(JSODIMM1-VSS-Pad201) -> GND
- JSODIMM1 pad 202: unconnected-(JSODIMM1-VSS-Pad202) -> GND
- JSODIMM1 pad 205: unconnected-(JSODIMM1-VSS-Pad205) -> GND
- JSODIMM1 pad 206: unconnected-(JSODIMM1-VSS-Pad206) -> GND
- JSODIMM1 pad 209: unconnected-(JSODIMM1-VSS-Pad209) -> GND
- JSODIMM1 pad 210: unconnected-(JSODIMM1-VSS-Pad210) -> GND
- JSODIMM1 pad 213: unconnected-(JSODIMM1-VSS-Pad213) -> GND
- JSODIMM1 pad 214: unconnected-(JSODIMM1-VSS-Pad214) -> GND
- JSODIMM1 pad 217: unconnected-(JSODIMM1-VSS-Pad217) -> GND
- JSODIMM1 pad 218: unconnected-(JSODIMM1-VSS-Pad218) -> GND
- JSODIMM1 pad 22: unconnected-(JSODIMM1-VSS-Pad22) -> GND
- JSODIMM1 pad 222: unconnected-(JSODIMM1-VSS-Pad222) -> GND
- JSODIMM1 pad 223: unconnected-(JSODIMM1-VSS-Pad223) -> GND
- JSODIMM1 pad 226: unconnected-(JSODIMM1-VSS-Pad226) -> GND
- JSODIMM1 pad 227: unconnected-(JSODIMM1-VSS-Pad227) -> GND
- JSODIMM1 pad 23: unconnected-(JSODIMM1-VSS-Pad23) -> GND
- JSODIMM1 pad 230: unconnected-(JSODIMM1-VSS-Pad230) -> GND
- JSODIMM1 pad 231: unconnected-(JSODIMM1-VSS-Pad231) -> GND
- JSODIMM1 pad 234: unconnected-(JSODIMM1-VSS-Pad234) -> GND
- JSODIMM1 pad 235: unconnected-(JSODIMM1-VSS-Pad235) -> GND
- JSODIMM1 pad 238: unconnected-(JSODIMM1-VSS-Pad238) -> GND
- JSODIMM1 pad 239: unconnected-(JSODIMM1-VSS-Pad239) -> GND
- JSODIMM1 pad 243: unconnected-(JSODIMM1-VSS-Pad243) -> GND
- JSODIMM1 pad 244: unconnected-(JSODIMM1-VSS-Pad244) -> GND
- JSODIMM1 pad 247: unconnected-(JSODIMM1-VSS-Pad247) -> GND
- JSODIMM1 pad 248: unconnected-(JSODIMM1-VSS-Pad248) -> GND
- JSODIMM1 pad 251: unconnected-(JSODIMM1-VSS-Pad251) -> GND
- JSODIMM1 pad 252: unconnected-(JSODIMM1-VSS-Pad252) -> GND
- JSODIMM1 pad 26: unconnected-(JSODIMM1-VSS-Pad26) -> GND
- JSODIMM1 pad 27: unconnected-(JSODIMM1-VSS-Pad27) -> GND
- JSODIMM1 pad 30: unconnected-(JSODIMM1-VSS-Pad30) -> GND
- JSODIMM1 pad 31: unconnected-(JSODIMM1-VSS-Pad31) -> GND
- JSODIMM1 pad 35: unconnected-(JSODIMM1-VSS-Pad35) -> GND
- JSODIMM1 pad 36: unconnected-(JSODIMM1-VSS-Pad36) -> GND
- JSODIMM1 pad 39: unconnected-(JSODIMM1-VSS-Pad39) -> GND
- JSODIMM1 pad 40: unconnected-(JSODIMM1-VSS-Pad40) -> GND
- JSODIMM1 pad 43: unconnected-(JSODIMM1-VSS-Pad43) -> GND
- JSODIMM1 pad 44: unconnected-(JSODIMM1-VSS-Pad44) -> GND
- JSODIMM1 pad 47: unconnected-(JSODIMM1-VSS-Pad47) -> GND
- JSODIMM1 pad 48: unconnected-(JSODIMM1-VSS-Pad48) -> GND
- JSODIMM1 pad 5: unconnected-(JSODIMM1-VSS-Pad5) -> GND
- JSODIMM1 pad 51: unconnected-(JSODIMM1-VSS-Pad51) -> GND
- JSODIMM1 pad 52: unconnected-(JSODIMM1-VSS-Pad52) -> GND
- JSODIMM1 pad 56: unconnected-(JSODIMM1-VSS-Pad56) -> GND
- JSODIMM1 pad 57: unconnected-(JSODIMM1-VSS-Pad57) -> GND
- JSODIMM1 pad 6: unconnected-(JSODIMM1-VSS-Pad6) -> GND
- JSODIMM1 pad 60: unconnected-(JSODIMM1-VSS-Pad60) -> GND
- JSODIMM1 pad 61: unconnected-(JSODIMM1-VSS-Pad61) -> GND
- JSODIMM1 pad 64: unconnected-(JSODIMM1-VSS-Pad64) -> GND
- JSODIMM1 pad 65: unconnected-(JSODIMM1-VSS-Pad65) -> GND
- JSODIMM1 pad 68: unconnected-(JSODIMM1-VSS-Pad68) -> GND
- JSODIMM1 pad 69: unconnected-(JSODIMM1-VSS-Pad69) -> GND
- JSODIMM1 pad 72: unconnected-(JSODIMM1-VSS-Pad72) -> GND
- JSODIMM1 pad 73: unconnected-(JSODIMM1-VSS-Pad73) -> GND
- JSODIMM1 pad 77: unconnected-(JSODIMM1-VSS-Pad77) -> GND
- JSODIMM1 pad 78: unconnected-(JSODIMM1-VSS-Pad78) -> GND
- JSODIMM1 pad 81: unconnected-(JSODIMM1-VSS-Pad81) -> GND
- JSODIMM1 pad 82: unconnected-(JSODIMM1-VSS-Pad82) -> GND
- JSODIMM1 pad 85: unconnected-(JSODIMM1-VSS-Pad85) -> GND
- JSODIMM1 pad 86: unconnected-(JSODIMM1-VSS-Pad86) -> GND
- JSODIMM1 pad 89: unconnected-(JSODIMM1-VSS-Pad89) -> GND
- JSODIMM1 pad 9: unconnected-(JSODIMM1-VSS-Pad9) -> GND
- JSODIMM1 pad 90: unconnected-(JSODIMM1-VSS-Pad90) -> GND
- JSODIMM1 pad 93: unconnected-(JSODIMM1-VSS-Pad93) -> GND
- JSODIMM1 pad 94: unconnected-(JSODIMM1-VSS-Pad94) -> GND
- JSODIMM1 pad 98: unconnected-(JSODIMM1-VSS-Pad98) -> GND
- JSODIMM1 pad 99: unconnected-(JSODIMM1-VSS-Pad99) -> GND
- JSODIMM1 pad MP1: unconnected-(JSODIMM1-PadMP1) -> GND
- JSODIMM1 pad MP2: unconnected-(JSODIMM1-PadMP2) -> GND
- JSODIMM2 pad 1: unconnected-(JSODIMM2-VSS-Pad1) -> GND
- JSODIMM2 pad 10: unconnected-(JSODIMM2-VSS-Pad10) -> GND
- JSODIMM2 pad 102: unconnected-(JSODIMM2-VSS-Pad102) -> GND
- JSODIMM2 pad 103: unconnected-(JSODIMM2-VSS-Pad103) -> GND
- JSODIMM2 pad 106: unconnected-(JSODIMM2-VSS-Pad106) -> GND
- JSODIMM2 pad 107: unconnected-(JSODIMM2-VSS-Pad107) -> GND
- JSODIMM2 pad 14: unconnected-(JSODIMM2-VSS-Pad14) -> GND
- JSODIMM2 pad 15: unconnected-(JSODIMM2-VSS-Pad15) -> GND
- JSODIMM2 pad 167: unconnected-(JSODIMM2-VSS-Pad167) -> GND
- JSODIMM2 pad 168: unconnected-(JSODIMM2-VSS-Pad168) -> GND
- JSODIMM2 pad 171: unconnected-(JSODIMM2-VSS-Pad171) -> GND
- JSODIMM2 pad 172: unconnected-(JSODIMM2-VSS-Pad172) -> GND
- JSODIMM2 pad 175: unconnected-(JSODIMM2-VSS-Pad175) -> GND
- JSODIMM2 pad 176: unconnected-(JSODIMM2-VSS-Pad176) -> GND
- JSODIMM2 pad 18: unconnected-(JSODIMM2-VSS-Pad18) -> GND
- JSODIMM2 pad 180: unconnected-(JSODIMM2-VSS-Pad180) -> GND
- JSODIMM2 pad 181: unconnected-(JSODIMM2-VSS-Pad181) -> GND
- JSODIMM2 pad 184: unconnected-(JSODIMM2-VSS-Pad184) -> GND
- JSODIMM2 pad 185: unconnected-(JSODIMM2-VSS-Pad185) -> GND
- JSODIMM2 pad 188: unconnected-(JSODIMM2-VSS-Pad188) -> GND
- JSODIMM2 pad 189: unconnected-(JSODIMM2-VSS-Pad189) -> GND
- JSODIMM2 pad 19: unconnected-(JSODIMM2-VSS-Pad19) -> GND
- JSODIMM2 pad 192: unconnected-(JSODIMM2-VSS-Pad192) -> GND
- JSODIMM2 pad 193: unconnected-(JSODIMM2-VSS-Pad193) -> GND
- JSODIMM2 pad 196: unconnected-(JSODIMM2-VSS-Pad196) -> GND
- JSODIMM2 pad 197: unconnected-(JSODIMM2-VSS-Pad197) -> GND
- JSODIMM2 pad 2: unconnected-(JSODIMM2-VSS-Pad2) -> GND
- JSODIMM2 pad 201: unconnected-(JSODIMM2-VSS-Pad201) -> GND
- JSODIMM2 pad 202: unconnected-(JSODIMM2-VSS-Pad202) -> GND
- JSODIMM2 pad 205: unconnected-(JSODIMM2-VSS-Pad205) -> GND
- JSODIMM2 pad 206: unconnected-(JSODIMM2-VSS-Pad206) -> GND
- JSODIMM2 pad 209: unconnected-(JSODIMM2-VSS-Pad209) -> GND
- JSODIMM2 pad 210: unconnected-(JSODIMM2-VSS-Pad210) -> GND
- JSODIMM2 pad 213: unconnected-(JSODIMM2-VSS-Pad213) -> GND
- JSODIMM2 pad 214: unconnected-(JSODIMM2-VSS-Pad214) -> GND
- JSODIMM2 pad 217: unconnected-(JSODIMM2-VSS-Pad217) -> GND
- JSODIMM2 pad 218: unconnected-(JSODIMM2-VSS-Pad218) -> GND
- JSODIMM2 pad 22: unconnected-(JSODIMM2-VSS-Pad22) -> GND
- JSODIMM2 pad 222: unconnected-(JSODIMM2-VSS-Pad222) -> GND
- JSODIMM2 pad 223: unconnected-(JSODIMM2-VSS-Pad223) -> GND
- JSODIMM2 pad 226: unconnected-(JSODIMM2-VSS-Pad226) -> GND
- JSODIMM2 pad 227: unconnected-(JSODIMM2-VSS-Pad227) -> GND
- JSODIMM2 pad 23: unconnected-(JSODIMM2-VSS-Pad23) -> GND
- JSODIMM2 pad 230: unconnected-(JSODIMM2-VSS-Pad230) -> GND
- JSODIMM2 pad 231: unconnected-(JSODIMM2-VSS-Pad231) -> GND
- JSODIMM2 pad 234: unconnected-(JSODIMM2-VSS-Pad234) -> GND
- JSODIMM2 pad 235: unconnected-(JSODIMM2-VSS-Pad235) -> GND
- JSODIMM2 pad 238: unconnected-(JSODIMM2-VSS-Pad238) -> GND
- JSODIMM2 pad 239: unconnected-(JSODIMM2-VSS-Pad239) -> GND
- JSODIMM2 pad 243: unconnected-(JSODIMM2-VSS-Pad243) -> GND
- JSODIMM2 pad 244: unconnected-(JSODIMM2-VSS-Pad244) -> GND
- JSODIMM2 pad 247: unconnected-(JSODIMM2-VSS-Pad247) -> GND
- JSODIMM2 pad 248: unconnected-(JSODIMM2-VSS-Pad248) -> GND
- JSODIMM2 pad 251: unconnected-(JSODIMM2-VSS-Pad251) -> GND
- JSODIMM2 pad 252: unconnected-(JSODIMM2-VSS-Pad252) -> GND
- JSODIMM2 pad 26: unconnected-(JSODIMM2-VSS-Pad26) -> GND
- JSODIMM2 pad 27: unconnected-(JSODIMM2-VSS-Pad27) -> GND
- JSODIMM2 pad 30: unconnected-(JSODIMM2-VSS-Pad30) -> GND
- JSODIMM2 pad 31: unconnected-(JSODIMM2-VSS-Pad31) -> GND
- JSODIMM2 pad 35: unconnected-(JSODIMM2-VSS-Pad35) -> GND
- JSODIMM2 pad 36: unconnected-(JSODIMM2-VSS-Pad36) -> GND
- JSODIMM2 pad 39: unconnected-(JSODIMM2-VSS-Pad39) -> GND
- JSODIMM2 pad 40: unconnected-(JSODIMM2-VSS-Pad40) -> GND
- JSODIMM2 pad 43: unconnected-(JSODIMM2-VSS-Pad43) -> GND
- JSODIMM2 pad 44: unconnected-(JSODIMM2-VSS-Pad44) -> GND
- JSODIMM2 pad 47: unconnected-(JSODIMM2-VSS-Pad47) -> GND
- JSODIMM2 pad 48: unconnected-(JSODIMM2-VSS-Pad48) -> GND
- JSODIMM2 pad 5: unconnected-(JSODIMM2-VSS-Pad5) -> GND
- JSODIMM2 pad 51: unconnected-(JSODIMM2-VSS-Pad51) -> GND
- JSODIMM2 pad 52: unconnected-(JSODIMM2-VSS-Pad52) -> GND
- JSODIMM2 pad 56: unconnected-(JSODIMM2-VSS-Pad56) -> GND
- JSODIMM2 pad 57: unconnected-(JSODIMM2-VSS-Pad57) -> GND
- JSODIMM2 pad 6: unconnected-(JSODIMM2-VSS-Pad6) -> GND
- JSODIMM2 pad 60: unconnected-(JSODIMM2-VSS-Pad60) -> GND
- JSODIMM2 pad 61: unconnected-(JSODIMM2-VSS-Pad61) -> GND
- JSODIMM2 pad 64: unconnected-(JSODIMM2-VSS-Pad64) -> GND
- JSODIMM2 pad 65: unconnected-(JSODIMM2-VSS-Pad65) -> GND
- JSODIMM2 pad 68: unconnected-(JSODIMM2-VSS-Pad68) -> GND
- JSODIMM2 pad 69: unconnected-(JSODIMM2-VSS-Pad69) -> GND
- JSODIMM2 pad 72: unconnected-(JSODIMM2-VSS-Pad72) -> GND
- JSODIMM2 pad 73: unconnected-(JSODIMM2-VSS-Pad73) -> GND
- JSODIMM2 pad 77: unconnected-(JSODIMM2-VSS-Pad77) -> GND
- JSODIMM2 pad 78: unconnected-(JSODIMM2-VSS-Pad78) -> GND
- JSODIMM2 pad 81: unconnected-(JSODIMM2-VSS-Pad81) -> GND
- JSODIMM2 pad 82: unconnected-(JSODIMM2-VSS-Pad82) -> GND
- JSODIMM2 pad 85: unconnected-(JSODIMM2-VSS-Pad85) -> GND
- JSODIMM2 pad 86: unconnected-(JSODIMM2-VSS-Pad86) -> GND
- JSODIMM2 pad 89: unconnected-(JSODIMM2-VSS-Pad89) -> GND
- JSODIMM2 pad 9: unconnected-(JSODIMM2-VSS-Pad9) -> GND
- JSODIMM2 pad 90: unconnected-(JSODIMM2-VSS-Pad90) -> GND
- JSODIMM2 pad 93: unconnected-(JSODIMM2-VSS-Pad93) -> GND
- JSODIMM2 pad 94: unconnected-(JSODIMM2-VSS-Pad94) -> GND
- JSODIMM2 pad 98: unconnected-(JSODIMM2-VSS-Pad98) -> GND
- JSODIMM2 pad 99: unconnected-(JSODIMM2-VSS-Pad99) -> GND
- JSODIMM2 pad MP1: unconnected-(JSODIMM2-PadMP1) -> GND
- JSODIMM2 pad MP2: unconnected-(JSODIMM2-PadMP2) -> GND
